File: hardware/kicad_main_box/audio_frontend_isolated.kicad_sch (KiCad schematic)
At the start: 3 parts, among them Q1 TLP222A, T1 LM-NP-1001, T2 LM-NP-1001

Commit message: hardware(schematic): assign exact footprints to all hierarchical schematic symbols
- Assign SMD footprints for ESP32-S3, ES8388, TCAN334G, LM5164-Q1, TPS7A0533
- Assign footprints for Bourns LM-NP-1001 transformers, TLP222A PhotoMOS, TVS, passives, and IDC26 connector
- Fix F8 PCB netlist synchronization (0 unassigned footprint errors)
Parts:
- Q1: footprint (none) -> Package_SO:Toshiba_SOIC-4-6_4.4x3.6mm_P1.27mm
- T1, T2: footprint (none) -> Transformer_SMD:Transformer_Ethernet_HALO_TG111-MSC13
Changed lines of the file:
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@@
 		(property "Reference" "T1" (at 120.0 42.0 0) (effects (font (size 1.27 1.27))))
 		(property "Value" "LM-NP-1001" (at 120.0 45.0 0) (effects (font (size 1.27 1.27))))
+		(property "Footprint" "Transformer_SMD:Transformer_Ethernet_HALO_TG111-MSC13" (at 0 0 0) (effects (font (size 1.27 1.27)) (hide yes)))
 		(pin "1")
 		(pin "2")
@@
 		(property "Reference" "T2" (at 120.0 62.0 0) (effects (font (size 1.27 1.27))))
 		(property "Value" "LM-NP-1001" (at 120.0 65.0 0) (effects (font (size 1.27 1.27))))
+		(property "Footprint" "Transformer_SMD:Transformer_Ethernet_HALO_TG111-MSC13" (at 0 0 0) (effects (font (size 1.27 1.27)) (hide yes)))
 		(pin "1")
 		(pin "2")
@@
 		(property "Reference" "Q1" (at 120.0 102.0 0) (effects (font (size 1.27 1.27))))
 		(property "Value" "TLP222A" (at 120.0 105.0 0) (effects (font (size 1.27 1.27))))
+		(property "Footprint" "Package_SO:Toshiba_SOIC-4-6_4.4x3.6mm_P1.27mm" (at 0 0 0) (effects (font (size 1.27 1.27)) (hide yes)))
 		(pin "1")
 		(pin "2")

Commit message: hardware(schematic): align TLP222A symbol pin numbers (1,3,4,6) with Toshiba SOIC-4-6 footprint
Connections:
- net POD1_OPTO: now also Q1.6 (DRAIN2); no longer Q1.4 (DRAIN2)
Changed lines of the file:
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@@
 		(property "Footprint" "Package_SO:Toshiba_SOIC-4-6_4.4x3.6mm_P1.27mm" (at 0 0 0) (effects (font (size 1.27 1.27)) (hide yes)))
 		(pin "1")
-		(pin "2")
 		(pin "3")
 		(pin "4")
+		(pin "6")
 	)
 	(wire (pts (xy 30.0 50.0) (xy 112.38 52.54)) (stroke (width 0) (type solid)))

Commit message: hardware(schematic): align schematic reference designators with PCB layout
- Rename Q1 -> U7 in audio_frontend_isolated (TLP222A Opto1)
- Rename U7 -> U9 in power_supply_ups (TPS7A0533 LDO)
- Rename D1 -> D2 in power_supply_ups (SMBJ33CA TVS)
- Fix 100% 1:1 symbol-to-PCB reference mapping (0 unplaced ghost components on mouse cursor)
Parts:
- renumbered Q1 to U7
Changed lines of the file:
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@@
 	(symbol (lib_id "Relay:TLP222A") (at 120.0 110.0 0) (unit 1)
 		(in_bom yes) (on_board yes) (dnp no)
-		(property "Reference" "Q1" (at 120.0 102.0 0) (effects (font (size 1.27 1.27))))
+		(property "Reference" "U7" (at 120.0 102.0 0) (effects (font (size 1.27 1.27))))
 		(property "Value" "TLP222A" (at 120.0 105.0 0) (effects (font (size 1.27 1.27))))
 		(property "Footprint" "Package_SO:Toshiba_SOIC-4-6_4.4x3.6mm_P1.27mm" (at 0 0 0) (effects (font (size 1.27 1.27)) (hide yes)))

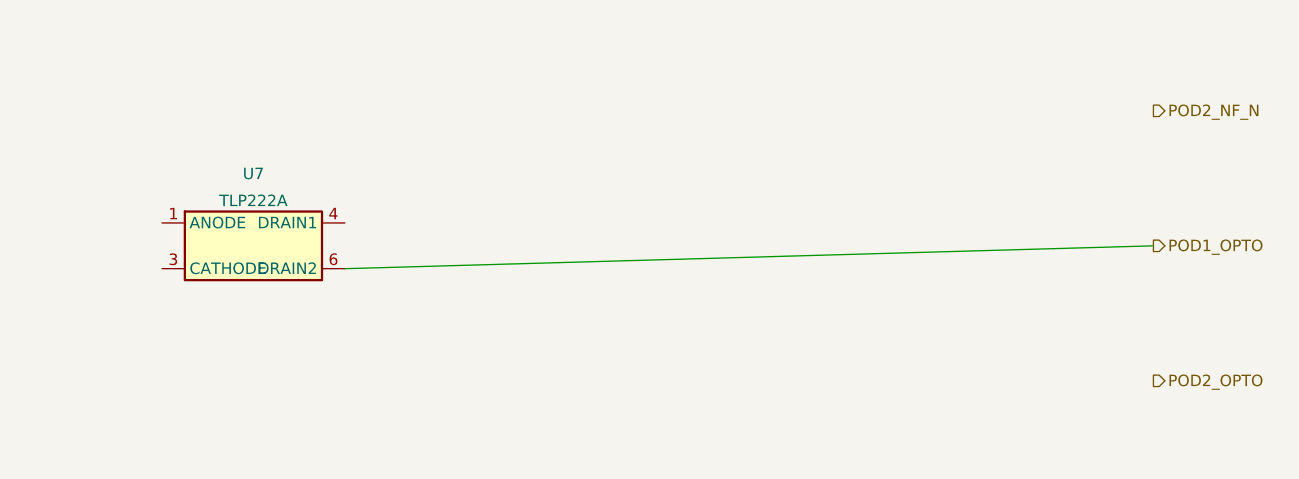
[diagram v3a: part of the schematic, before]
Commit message: feat(arch): finalize v8.5/v9.0 Clean All-UWB Architecture, 6-PCBA lineup and Pure-DC wiring in documentation
- All-UWB Interconnects: Central Box communicates with Front-Node, Bay 1 (Left), Bay 2 (Right), and Rear Radar strictly over Qorvo DW3110 UWB (6.489 GHz Ch. 5, <0.4 ms latency, AES-128-CCM).
- Symmetrical Mounting Bays: Pod 1 and Pod 2 are physical docking bays (Bucht 1 / Bucht 2, Left / Right) for gateway units, NOT Fahrer / Sozius. Rider and pillion helmets connect directly via Bluetooth to Central Box DSP.
- 6-PCBA Lineup: PCBA 02 (Pod Base) and PCBA 04 (Rear Pod 3) retired and archived. Pod enclosures use direct 2-wire DC leaf spring contacts (+5V/GND). PCBA 03 is 2-sided SMT with DW3110, Host-MCU, and 4x AO3400A MOSFETs.
- Deutsch DTM-12 Harness: Replaced HD26 connector with 12-pin Deutsch DTM-12 automotive connector providing pure DC power.
- Power Sequencing & Roaming: Boot sequence (T=0, 200, 350, 500 ms), HW button SW1 (pairing & NVS reset), and 4-vehicle NVS roaming.
- Documentation Updated: docs/de/ 01, 03, 04, 07, 08, 09, 13, 14, 15, 16, status.md, DECISIONS_LOG.md (ADR-011), and hardware/README.md.
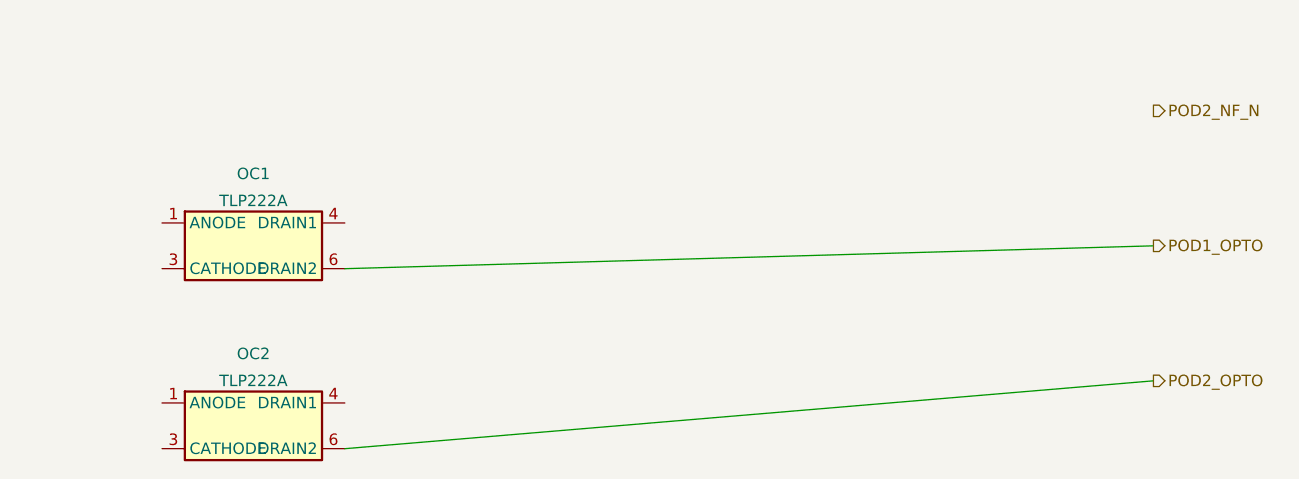
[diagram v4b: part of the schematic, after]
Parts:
- added OC2: TLP222A, Package_SO:Toshiba_SOIC-4-6_4.4x3.6mm_P1.27mm, symbol Relay:TLP222A
- OC1: renamed from U7; LCSC (none) -> C112444
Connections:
- net POD2_OPTO: now also OC2.6 (DRAIN2)
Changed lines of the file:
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@@
 	(symbol (lib_id "Relay:TLP222A") (at 120.0 110.0 0) (unit 1)
 		(in_bom yes) (on_board yes) (dnp no)
-		(property "Reference" "U7" (at 120.0 102.0 0) (effects (font (size 1.27 1.27))))
+		(property "Reference" "OC1" (at 120.0 102.0 0) (effects (font (size 1.27 1.27))))
 		(property "Value" "TLP222A" (at 120.0 105.0 0) (effects (font (size 1.27 1.27))))
 		(property "Footprint" "Package_SO:Toshiba_SOIC-4-6_4.4x3.6mm_P1.27mm" (at 0 0 0) (effects (font (size 1.27 1.27)) (hide yes)))
+		(property "LCSC" "C112444" (at 0 0 0) (effects (font (size 1.27 1.27)) (hide yes)))
+		(pin "1")
+		(pin "3")
+		(pin "4")
+		(pin "6")
+	)
+	(symbol (lib_id "Relay:TLP222A") (at 120.0 130.0 0) (unit 1)
+		(in_bom yes) (on_board yes) (dnp no)
+		(property "Reference" "OC2" (at 120.0 122.0 0) (effects (font (size 1.27 1.27))))
+		(property "Value" "TLP222A" (at 120.0 125.0 0) (effects (font (size 1.27 1.27))))
+		(property "Footprint" "Package_SO:Toshiba_SOIC-4-6_4.4x3.6mm_P1.27mm" (at 0 0 0) (effects (font (size 1.27 1.27)) (hide yes)))
+		(property "LCSC" "C112444" (at 0 0 0) (effects (font (size 1.27 1.27)) (hide yes)))
 		(pin "1")
 		(pin "3")
@@
 	(wire (pts (xy 127.62 72.54) (xy 220.0 65.0)) (stroke (width 0) (type solid)))
 	(wire (pts (xy 130.16 112.54) (xy 220.0 110.0)) (stroke (width 0) (type solid)))
+	(wire (pts (xy 130.16 132.54) (xy 220.0 125.0)) (stroke (width 0) (type solid)))
 )

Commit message: hardware(cartridge): move ES8388 audio codec to B.Cu bottom layer to eliminate overlaps and isolate from actuator MOSFETs
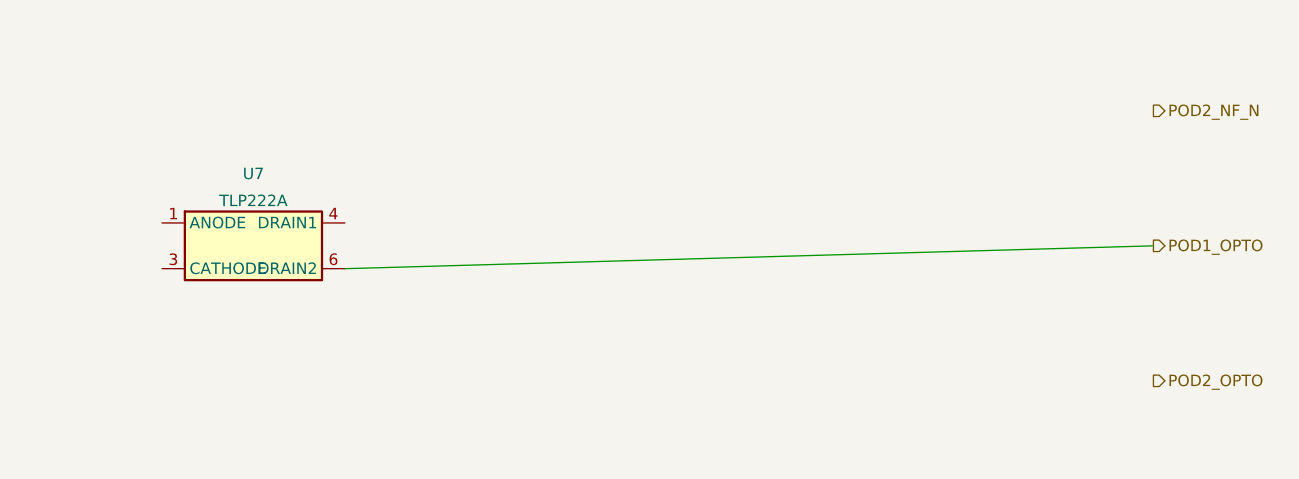
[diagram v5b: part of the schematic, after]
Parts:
- removed OC2: TLP222A, Package_SO:Toshiba_SOIC-4-6_4.4x3.6mm_P1.27mm, symbol Relay:TLP222A
- U7: renamed from OC1; LCSC C112444 -> (none)
